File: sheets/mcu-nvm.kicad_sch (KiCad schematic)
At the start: 49 parts

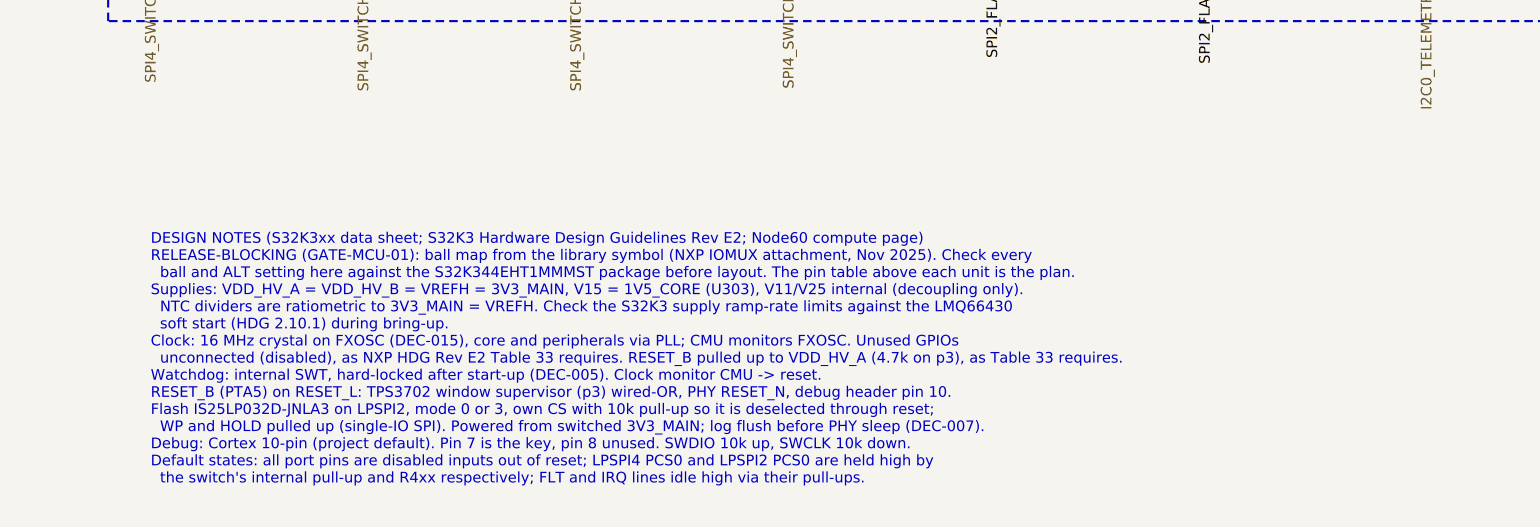
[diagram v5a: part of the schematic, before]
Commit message: GATE-MCU-01 passed: S32K344 package map audit
All 257 U401 balls cross-checked against NXP's IOMUX table (RM, Nov
2025), the 257BGA IBIS model and BSDL file (HW design package Rev. E2):
no differences; every used signal has its planned function on its
ball. The user signed off on 2026-10-28.

- gates.yaml: status passed, result page validation/gate-mcu-01
- Result page with method and the schematic's pin plan (NXP select
  values stay in the private review sheet)
- Compute page, parts.yaml, CLAUDE.md and the p4 note updated

Co-Authored-By: Claude Opus 5.5 <noreply@anthropic.com>
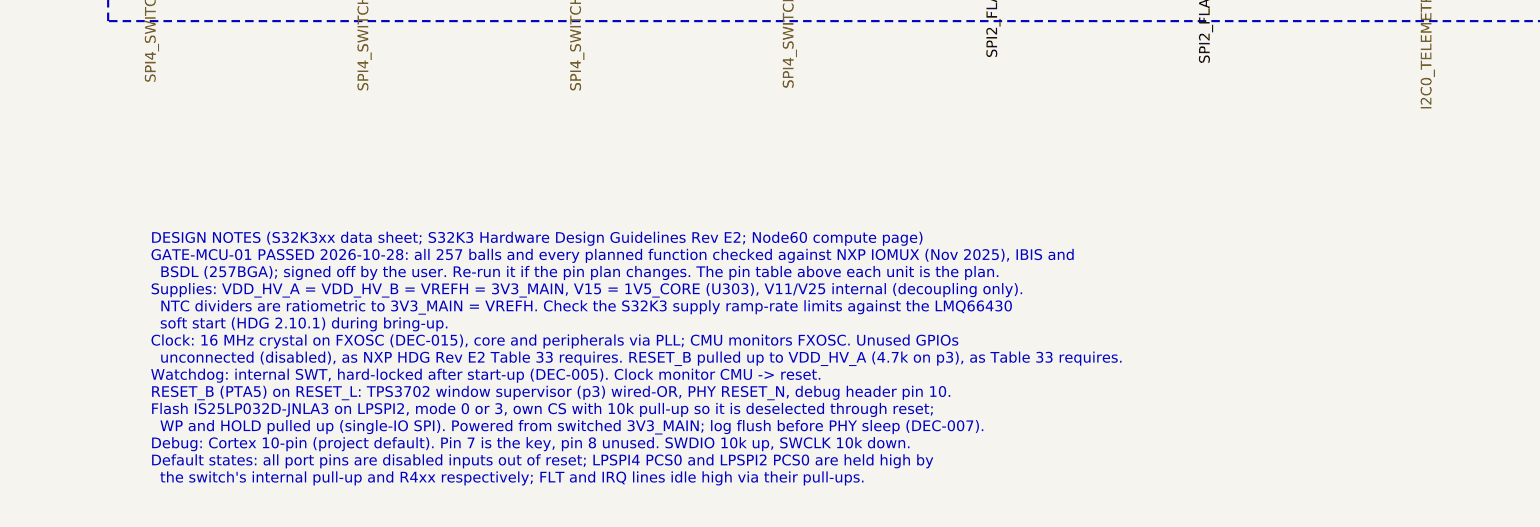
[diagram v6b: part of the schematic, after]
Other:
- note added: "DESIGN NOTES (S32K3xx data sheet; S32K3 Hardware Design Guidelines Rev E2; Node60 compute page) GATE-MCU-01 PASSED 2026-10-28: all 257 balls and every planned function checked against NXP IOMUX (Nov 2025), IBIS and BSDL (257BGA); signed off by the user. Re-run it if the pin plan changes. The pin table above each unit is the plan. Supplies: VDD_HV_A = VDD_HV_B = VREFH = 3V3_MAIN, V15 = 1V5_CORE (U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"
- note removed: "DESIGN NOTES (S32K3xx data sheet; S32K3 Hardware Design Guidelines Rev E2; Node60 compute page) RELEASE-BLOCKING (GATE-MCU-01): ball map from the library symbol (NXP IOMUX attachment, Nov 2025). Check every ball and ALT setting here against the S32K344EHT1MMMST package before layout. The pin table above each unit is the plan. Supplies: VDD_HV_A = VDD_HV_B = VREFH = 3V3_MAIN, V15 = 1V5_CORE (U303)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"
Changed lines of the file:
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@@
 		)
 	)
-	(text "DESIGN NOTES (S32K3xx data sheet; S32K3 Hardware Design Guidelines Rev E2; Node60 compute page)\nRELEASE-BLOCKING (GATE-MCU-01): ball map from the library symbol (NXP IOMUX attachment, Nov 2025). Check every\n  ball and ALT setting here against the S32K344EHT1MMMST package before layout. The pin table above each unit is the plan.\nSupplies: VDD_HV_A = VDD_HV_B = VREFH = 3V3_MAIN, V15 = 1V5_CORE (U303), V11/V25 internal (decoupling only).\n  NTC dividers are ratiometric to 3V3_MAIN = VREFH. Check the S32K3 supply ramp-rate limits against the LMQ66430\n  soft start (HDG 2.10.1) during bring-up.\nClock: 16 MHz crystal on FXOSC (DEC-015), core and peripherals via PLL; CMU monitors FXOSC. Unused GPIOs\n  unconnected (disabled), as NXP HDG Rev E2 Table 33 requires. RESET_B pulled up to VDD_HV_A (4.7k on p3), as Table 33 requires.\nWatchdog: internal SWT, hard-locked after start-up (DEC-005). Clock monitor CMU -> reset.\nRESET_B (PTA5) on RESET_L: TPS3702 window supervisor (p3) wired-OR, PHY RESET_N, debug header pin 10.\nFlash IS25LP032D-JNLA3 on LPSPI2, mode 0 or 3, own CS with 10k pull-up so it is deselected through reset;\n  WP and HOLD pulled up (single-IO SPI). Powered from switched 3V3_MAIN; log flush before PHY sleep (DEC-007).\nDebug: Cortex 10-pin (project default). Pin 7 is the key, pin 8 unused. SWDIO 10k up, SWCLK 10k down.\nDefault states: all port pins are disabled inputs out of reset; LPSPI4 PCS0 and LPSPI2 PCS0 are held high by\n  the switch's internal pull-up and R4xx respectively; FLT and IRQ lines idle high via their pull-ups.\n"
+	(text "DESIGN NOTES (S32K3xx data sheet; S32K3 Hardware Design Guidelines Rev E2; Node60 compute page)\nGATE-MCU-01 PASSED 2026-10-28: all 257 balls and every planned function checked against NXP IOMUX (Nov 2025), IBIS and\n  BSDL (257BGA); signed off by the user. Re-run it if the pin plan changes. The pin table above each unit is the plan.\nSupplies: VDD_HV_A = VDD_HV_B = VREFH = 3V3_MAIN, V15 = 1V5_CORE (U303), V11/V25 internal (decoupling only).\n  NTC dividers are ratiometric to 3V3_MAIN = VREFH. Check the S32K3 supply ramp-rate limits against the LMQ66430\n  soft start (HDG 2.10.1) during bring-up.\nClock: 16 MHz crystal on FXOSC (DEC-015), core and peripherals via PLL; CMU monitors FXOSC. Unused GPIOs\n  unconnected (disabled), as NXP HDG Rev E2 Table 33 requires. RESET_B pulled up to VDD_HV_A (4.7k on p3), as Table 33 requires.\nWatchdog: internal SWT, hard-locked after start-up (DEC-005). Clock monitor CMU -> reset.\nRESET_B (PTA5) on RESET_L: TPS3702 window supervisor (p3) wired-OR, PHY RESET_N, debug header pin 10.\nFlash IS25LP032D-JNLA3 on LPSPI2, mode 0 or 3, own CS with 10k pull-up so it is deselected through reset;\n  WP and HOLD pulled up (single-IO SPI). Powered from switched 3V3_MAIN; log flush before PHY sleep (DEC-007).\nDebug: Cortex 10-pin (project default). Pin 7 is the key, pin 8 unused. SWDIO 10k up, SWCLK 10k down.\nDefault states: all port pins are disabled inputs out of reset; LPSPI4 PCS0 and LPSPI2 PCS0 are held high by\n  the switch's internal pull-up and R4xx respectively; FLT and IRQ lines idle high via their pull-ups.\n"
 		(exclude_from_sim no)
 		(at 236.22 368.3 0)

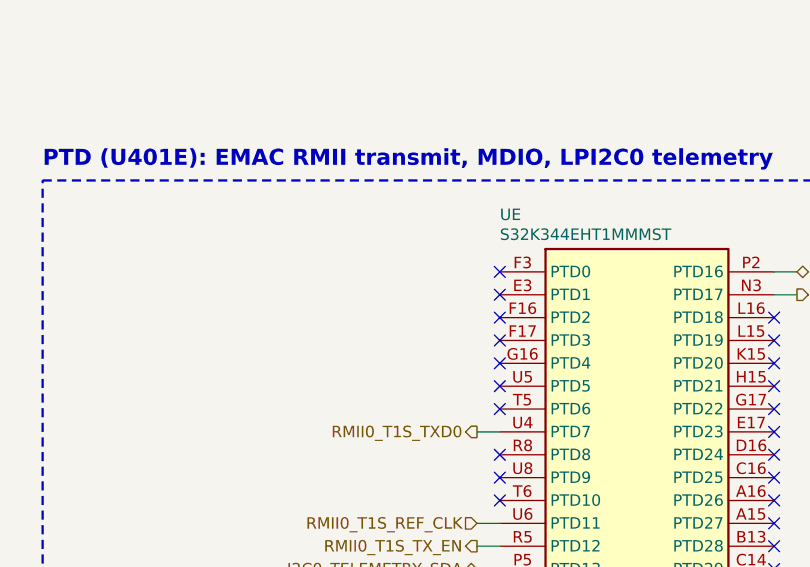
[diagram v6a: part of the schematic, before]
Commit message: DEC-017: T1S bus pass-through and relay-switched termination
The user asked for a second T1S connector so a downstream node can join
the bus, and a termination that can be switched between bus end and
mid-bus (2026-10-28).

- p9: J912, a second ATM13-2P-BM04 in parallel with J903
- p5: R502 (single 100R, not fitted) replaced by the OPEN Alliance
  split termination: latching relay K501 (Omron G6KU-2F-Y-T1-TRS DC3,
  +125 °C) selects 49.9R (end, SET) or 1.5k (drop, RESET) legs to a
  centre tap with 100nF || 100k; Q501/Q502 (DMC2710UVQ-7) half-bridges
  drive the coil from 3V3_MAIN
- p4/root: PTD0 -> T1S_TERM_END, PTD1 -> T1S_TERM_DROP
- Library pinned to dropout-kicad-library PR #37 head db07592; the new
  DropOut_Relay / DropOut_Relay_SMD libraries are in the library tables
- DEC-017, parts, GATE-NET-02 (switched termination), GATE-NET-01 wake
  test in both states, firmware and network pages, GATE-MCU-01 addendum

Co-Authored-By: Claude Opus 5.5 <noreply@anthropic.com>
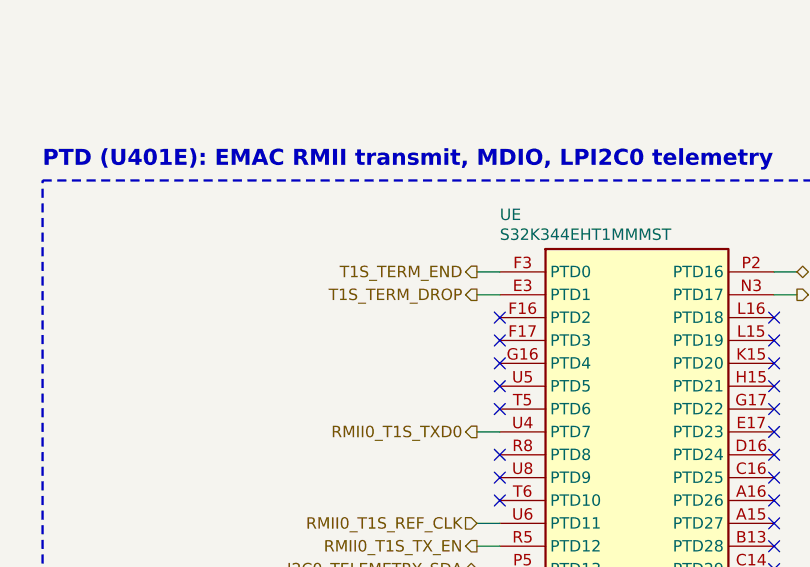
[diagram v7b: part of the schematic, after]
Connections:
- net T1S_TERM_DROP: now reaches U.E3 (PTD1)
- net T1S_TERM_END: now reaches U.F3 (PTD0)
- no-connect marks 179 -> 177
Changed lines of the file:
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@@
 	)
 	(no_connect
-		(at 355.6 203.2)
-	)
-	(no_connect
 		(at 386.08 218.44)
 	)
 	(no_connect
-		(at 355.6 200.66)
-	)
-	(no_connect
 		(at 355.6 205.74)
 	)
@@
 		)
 	)
+	(wire
+		(pts
+			(xy 355.6 200.66)
+			(xy 353.06 200.66)
+		)
+		(stroke
+			(width 0)
+			(type default)
+		)
+	)
+	(hierarchical_label "T1S_TERM_END"
+		(shape output)
+		(at 353.06 200.66 180)
+		(effects
+			(font
+				(size 1.27 1.27)
+			)
+			(justify right)
+		)
+	)
+	(wire
+		(pts
+			(xy 355.6 203.2)
+			(xy 353.06 203.2)
+		)
+		(stroke
+			(width 0)
+			(type default)
+		)
+	)
+	(hierarchical_label "T1S_TERM_DROP"
+		(shape output)
+		(at 353.06 203.2 180)
+		(effects
+			(font
+				(size 1.27 1.27)
+			)
+			(justify right)
+		)
+	)

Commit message: One LPSPI bus per output switch (DEC-018); Zephyr as core RTOS (DEC-019)
- Split the TPS2HCS08A daisy chain into three buses: U601 on LPSPI4 (Rev A
  balls), U701 on LPSPI5 (A16/A15/B13/G16), U801 on LPSPI3 (E14/F14/E15/G15).
  The output-switch sheet now exposes generic SDI/SDO/SCK/CS_L ports.
- Per-switch SPI watchdog (400 ms) with limp-home off: a lost bus turns only
  that switch's two outputs off.
- DEC-019 records Zephyr with a driver map; pin plan reviewed against
  upstream Zephyr (EIRQ map, ADC group-channel, native PCS). No other pin moves.
- GATE-MCU-01 reopened for the eight new balls (IBIS/BSDL machine check done,
  user sign-off pending). Rev B (in progress) listed on the revisions page.

Co-Authored-By: Claude Opus 5.5 <noreply@anthropic.com>
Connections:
- net SPI5_SWITCH2_MOSI: now reaches U.A15 (PTD27)
- net SPI5_SWITCH2_SCK: now reaches U.A16 (PTD26)
- net SPI5_SWITCH2_MISO: now reaches U.B13 (PTD28)
- net SPI5_SWITCH2_CS_L: now reaches U.G16 (PTD4)
- net SPI3_SWITCH3_SCK: now reaches U.E14 (PTF13)
- net SPI3_SWITCH3_MISO: now reaches U.E15 (PTF12)
- net SPI3_SWITCH3_MOSI: now reaches U.F14 (PTF15)
- net SPI3_SWITCH3_CS_L: now reaches U.G15 (PTF16)
- net SPI4_SWITCH_CS_L renamed SPI4_SWITCH1_CS_L
- net SPI4_SWITCH_MISO renamed SPI4_SWITCH1_MISO
- net SPI4_SWITCH_MOSI renamed SPI4_SWITCH1_MOSI
- net SPI4_SWITCH_SCK renamed SPI4_SWITCH1_SCK
- no-connect marks 177 -> 169
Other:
- note added: "One LPSPI bus per TPS2HCS08 (DEC-018): LPSPI4 = U601, LPSPI5 = U701, LPSPI3 = U801. SPI mode 1 (CPOL 0, CPHA 1), 8 MHz max, 32-bit frames with CRC. Each PCS0 idles high from reset (switch internal pull-up): channels stay off until configured."
- note added: "PTB (U401C): LPSPI4: TPS2HCS08 U601 (outputs 1-2)"
- note added: "PTD (U401E): EMAC RMII transmit, MDIO, LPI2C0 telemetry, LPSPI5 U701 (outputs 3-4)"
- note added: "PTF (U401G): LPSPI2 flash MOSI, LPSPI3 U801 (outputs 5-6)"
- note removed: "LPSPI4 master, mode per TPS2HCS08 datasheet, 3 x 24-bit frames per CS with CRC. PCS0 must idle high from reset: switches keep all channels off until configured."
- note removed: "PTB (U401C): LPSPI4: TPS2HCS08 daisy chain"
- note removed: "PTD (U401E): EMAC RMII transmit, MDIO, LPI2C0 telemetry"
- note removed: "PTF (U401G): LPSPI2 flash MOSI"
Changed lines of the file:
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@@
 		)
 	)
-	(text "PTB (U401C): LPSPI4: TPS2HCS08 daisy chain"
+	(text "PTB (U401C): LPSPI4: TPS2HCS08 U601 (outputs 1-2)"
 		(exclude_from_sim no)
 		(at 454.66 77.47 0)
@@
 		)
 	)
-	(hierarchical_label "SPI4_SWITCH_CS_L"
+	(hierarchical_label "SPI4_SWITCH1_CS_L"
 		(shape output)
 		(at 502.92 109.22 180)
@@
 		)
 	)
-	(hierarchical_label "SPI4_SWITCH_MOSI"
+	(hierarchical_label "SPI4_SWITCH1_MOSI"
 		(shape output)
 		(at 502.92 111.76 180)
@@
 		)
 	)
-	(hierarchical_label "SPI4_SWITCH_MISO"
+	(hierarchical_label "SPI4_SWITCH1_MISO"
 		(shape input)
 		(at 502.92 116.84 180)
@@
 		)
 	)
-	(hierarchical_label "SPI4_SWITCH_SCK"
+	(hierarchical_label "SPI4_SWITCH1_SCK"
 		(shape output)
 		(at 502.92 114.3 180)
@@
 		)
 	)
-	(text "LPSPI4 master, mode per TPS2HCS08 datasheet, 3 x 24-bit frames per CS with CRC.\nPCS0 must idle high from reset: switches keep all channels off until configured."
+	(text "One LPSPI bus per TPS2HCS08 (DEC-018): LPSPI4 = U601, LPSPI5 = U701, LPSPI3 = U801.\nSPI mode 1 (CPOL 0, CPHA 1), 8 MHz max, 32-bit frames with CRC. Each PCS0 idles high from reset\n(switch internal pull-up): channels stay off until configured."
 		(exclude_from_sim no)
 		(at 457.2 137.16 0)
@@
 		)
 	)
-	(text "PTD (U401E): EMAC RMII transmit, MDIO, LPI2C0 telemetry"
+	(text "PTD (U401E): EMAC RMII transmit, MDIO, LPI2C0 telemetry, LPSPI5 U701 (outputs 3-4)"
 		(exclude_from_sim no)
 		(at 304.8 189.23 0)
@@
 		)
 	)
-	(no_connect
-		(at 386.08 228.6)
+	(wire
+		(pts
+			(xy 386.08 228.6)
+			(xy 388.62 228.6)
+		)
+		(stroke
+			(width 0)
+			(type default)
+		)
 	)
-	(no_connect
-		(at 386.08 226.06)
+	(hierarchical_label "SPI5_SWITCH2_MOSI"
+		(shape output)
+		(at 388.62 228.6 0)
+		(effects
+			(font
+				(size 1.27 1.27)
+			)
+			(justify left)
+		)
 	)
-	(no_connect
-		(at 386.08 231.14)
+	(wire
+		(pts
+			(xy 386.08 226.06)
+			(xy 388.62 226.06)
+		)
+		(stroke
+			(width 0)
+			(type default)
+		)
+	)
+	(hierarchical_label "SPI5_SWITCH2_SCK"
+		(shape output)
+		(at 388.62 226.06 0)
+		(effects
+			(font
+				(size 1.27 1.27)
+			)
+			(justify left)
+		)
+	)
+	(wire
+		(pts
+			(xy 386.08 231.14)
+			(xy 388.62 231.14)
+		)
+		(stroke
+			(width 0)
+			(type default)
+		)
+	)
+	(hierarchical_label "SPI5_SWITCH2_MISO"
+		(shape input)
+		(at 388.62 231.14 0)
+		(effects
+			(font
+				(size 1.27 1.27)
+			)
+			(justify left)
+		)
 	)
 	(no_connect
@@
 		(at 355.6 208.28)
 	)
-	(no_connect
-		(at 355.6 210.82)
+	(wire
+		(pts
+			(xy 355.6 210.82)
+			(xy 353.06 210.82)
+		)
+		(stroke
+			(width 0)
+			(type default)
+		)
+	)
+	(hierarchical_label "SPI5_SWITCH2_CS_L"
+		(shape output)
+		(at 353.06 210.82 180)
+		(effects
+			(font
+				(size 1.27 1.27)
+			)
+			(justify right)
+		)
 	)
 	(no_connect
@@
 		)
 	)
-	(text "PTF (U401G): LPSPI2 flash MOSI"
+	(text "PTF (U401G): LPSPI2 flash MOSI, LPSPI3 U801 (outputs 5-6)"
 		(exclude_from_sim no)
 		(at 604.52 189.23 0)
@@
 		(at 655.32 220.98)
 	)
-	(no_connect
-		(at 655.32 233.68)
+	(wire
+		(pts
+			(xy 655.32 233.68)
+			(xy 652.78 233.68)
+		)
+		(stroke
+			(width 0)
+			(type default)
+		)
 	)
-	(no_connect
-		(at 655.32 231.14)
+	(hierarchical_label "SPI3_SWITCH3_SCK"
+		(shape output)
+		(at 652.78 233.68 180)
+		(effects
+			(font
+				(size 1.27 1.27)
+			)
+			(justify right)
+		)
 	)
-	(no_connect
-		(at 655.32 238.76)
+	(wire
+		(pts
+			(xy 655.32 231.14)
+			(xy 652.78 231.14)
+		)
+		(stroke
+			(width 0)
+			(type default)
+		)
+	)
+	(hierarchical_label "SPI3_SWITCH3_MISO"
+		(shape input)
+		(at 652.78 231.14 180)
+		(effects
+			(font
+				(size 1.27 1.27)
+			)
+			(justify right)
+		)
+	)
+	(wire
+		(pts
+			(xy 655.32 238.76)
+			(xy 652.78 238.76)
+		)
+		(stroke
+			(width 0)
+			(type default)
+		)
+	)
+	(hierarchical_label "SPI3_SWITCH3_MOSI"
+		(shape output)
+		(at 652.78 238.76 180)
+		(effects
+			(font
+				(size 1.27 1.27)
+			)
+			(justify right)
+		)
 	)
 	(no_connect
@@
 		(at 685.8 203.2)
 	)
-	(no_connect
-		(at 685.8 200.66)
+	(wire
+		(pts
+			(xy 685.8 200.66)
+			(xy 688.34 200.66)
+		)
+		(stroke
+			(width 0)
+			(type default)
+		)
+	)
+	(hierarchical_label "SPI3_SWITCH3_CS_L"
+		(shape output)
+		(at 688.34 200.66 0)
+		(effects
+			(font
+				(size 1.27 1.27)
+			)
+			(justify left)
+		)
 	)
 	(no_connect
@@
 		)
 	)
-	(hierarchical_label "SPI4_SWITCH_SCK"
+	(hierarchical_label "SPI4_SWITCH1_SCK"
 		(shape output)
 		(at 236.22 332.74 270)
@@
 		)
 	)
-	(hierarchical_label "SPI4_SWITCH_MOSI"
+	(hierarchical_label "SPI4_SWITCH1_MOSI"
 		(shape output)
 		(at 261.62 332.74 270)
@@
 		)
 	)
-	(hierarchical_label "SPI4_SWITCH_MISO"
+	(hierarchical_label "SPI4_SWITCH1_MISO"
 		(shape input)
 		(at 287.02 332.74 270)
@@
 		)
 	)
-	(hierarchical_label "SPI4_SWITCH_CS_L"
+	(hierarchical_label "SPI4_SWITCH1_CS_L"
 		(shape output)
 		(at 312.42 332.74 270)
@@
 		)
 	)
-	(text "DESIGN NOTES (S32K3xx data sheet; S32K3 Hardware Design Guidelines Rev E2; Node60 compute page)\nGATE-MCU-01 PASSED 2026-10-28: all 257 balls and every planned function checked against NXP IOMUX (Nov 2025), IBIS and\n  BSDL (257BGA); signed off by the user. Re-run it if the pin plan changes. The pin table above each unit is the plan.\nSupplies: VDD_HV_A = VDD_HV_B = VREFH = 3V3_MAIN, V15 = 1V5_CORE (U303), V11/V25 internal (decoupling only).\n  NTC dividers are ratiometric to 3V3_MAIN = VREFH. Check the S32K3 supply ramp-rate limits against the LMQ66430\n  soft start (HDG 2.10.1) during bring-up.\nClock: 16 MHz crystal on FXOSC (DEC-015), core and peripherals via PLL; CMU monitors FXOSC. Unused GPIOs\n  unconnected (disabled), as NXP HDG Rev E2 Table 33 requires. RESET_B pulled up to VDD_HV_A (4.7k on p3), as Table 33 requires.\nWatchdog: internal SWT, hard-locked after start-up (DEC-005). Clock monitor CMU -> reset.\nRESET_B (PTA5) on RESET_L: TPS3702 window supervisor (p3) wired-OR, PHY RESET_N, debug header pin 10.\nFlash IS25LP032D-JNLA3 on LPSPI2, mode 0 or 3, own CS with 10k pull-up so it is deselected through reset;\n  WP and HOLD pulled up (single-IO SPI). Powered from switched 3V3_MAIN; log flush before PHY sleep (DEC-007).\nDebug: Cortex 10-pin (project default). Pin 7 is the key, pin 8 unused. SWDIO 10k up, SWCLK 10k down.\nDefault states: all port pins are disabled inputs out of reset; LPSPI4 PCS0 and LPSPI2 PCS0 are held high by\n  the switch's internal pull-up and R4xx respectively; FLT and IRQ lines idle high via their pull-ups.\n"
+	(text "DESIGN NOTES (S32K3xx data sheet; S32K3 Hardware Design Guidelines Rev E2; Node60 compute page)\nGATE-MCU-01 PASSED 2026-10-28: all 257 balls and every planned function checked against NXP IOMUX (Nov 2025), IBIS and\n  BSDL (257BGA); signed off by the user. Re-run it if the pin plan changes. The pin table above each unit is the plan.\nSupplies: VDD_HV_A = VDD_HV_B = VREFH = 3V3_MAIN, V15 = 1V5_CORE (U303), V11/V25 internal (decoupling only).\n  NTC dividers are ratiometric to 3V3_MAIN = VREFH. Check the S32K3 supply ramp-rate limits against the LMQ66430\n  soft start (HDG 2.10.1) during bring-up.\nClock: 16 MHz crystal on FXOSC (DEC-015), core and peripherals via PLL; CMU monitors FXOSC. Unused GPIOs\n  unconnected (disabled), as NXP HDG Rev E2 Table 33 requires. RESET_B pulled up to VDD_HV_A (4.7k on p3), as Table 33 requires.\nWatchdog: internal SWT, hard-locked after start-up (DEC-005). Clock monitor CMU -> reset.\nRESET_B (PTA5) on RESET_L: TPS3702 window supervisor (p3) wired-OR, PHY RESET_N, debug header pin 10.\nFlash IS25LP032D-JNLA3 on LPSPI2, mode 0 or 3, own CS with 10k pull-up so it is deselected through reset;\n  WP and HOLD pulled up (single-IO SPI). Powered from switched 3V3_MAIN; log flush before PHY sleep (DEC-007).\nDebug: Cortex 10-pin (project default). Pin 7 is the key, pin 8 unused. SWDIO 10k up, SWCLK 10k down.\nDefault states: all port pins are disabled inputs out of reset; LPSPI3/4/5 PCS0 and LPSPI2 PCS0 are held high by\n  each switch's internal pull-up and R4xx respectively; FLT and IRQ lines idle high via their pull-ups.\n"
 		(exclude_from_sim no)
 		(at 236.22 368.3 0)
